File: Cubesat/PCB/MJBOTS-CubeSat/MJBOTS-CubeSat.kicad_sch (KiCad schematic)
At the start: 11 parts, among them J1 Li 24V Battery, J2 MPU 6050, J3 Conn_01x08, J4 Conn_02x20_Odd_Even, U1 LM2596S

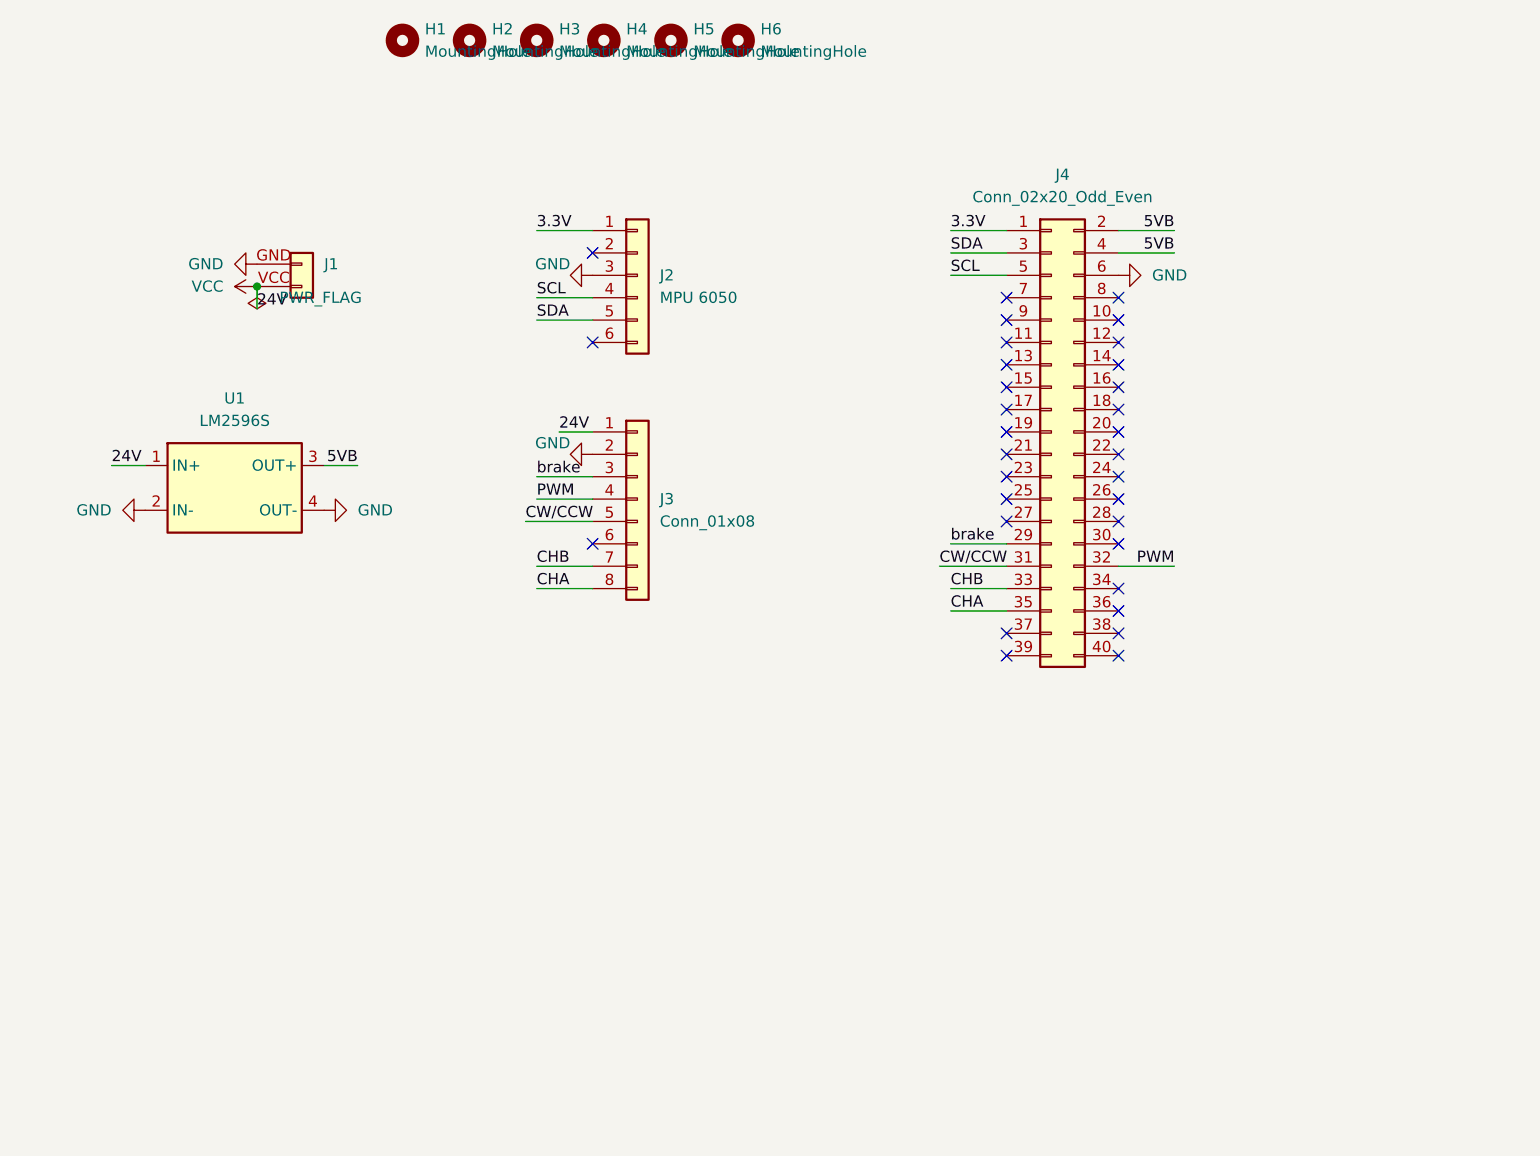
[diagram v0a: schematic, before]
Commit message: Updated Moteus PCB
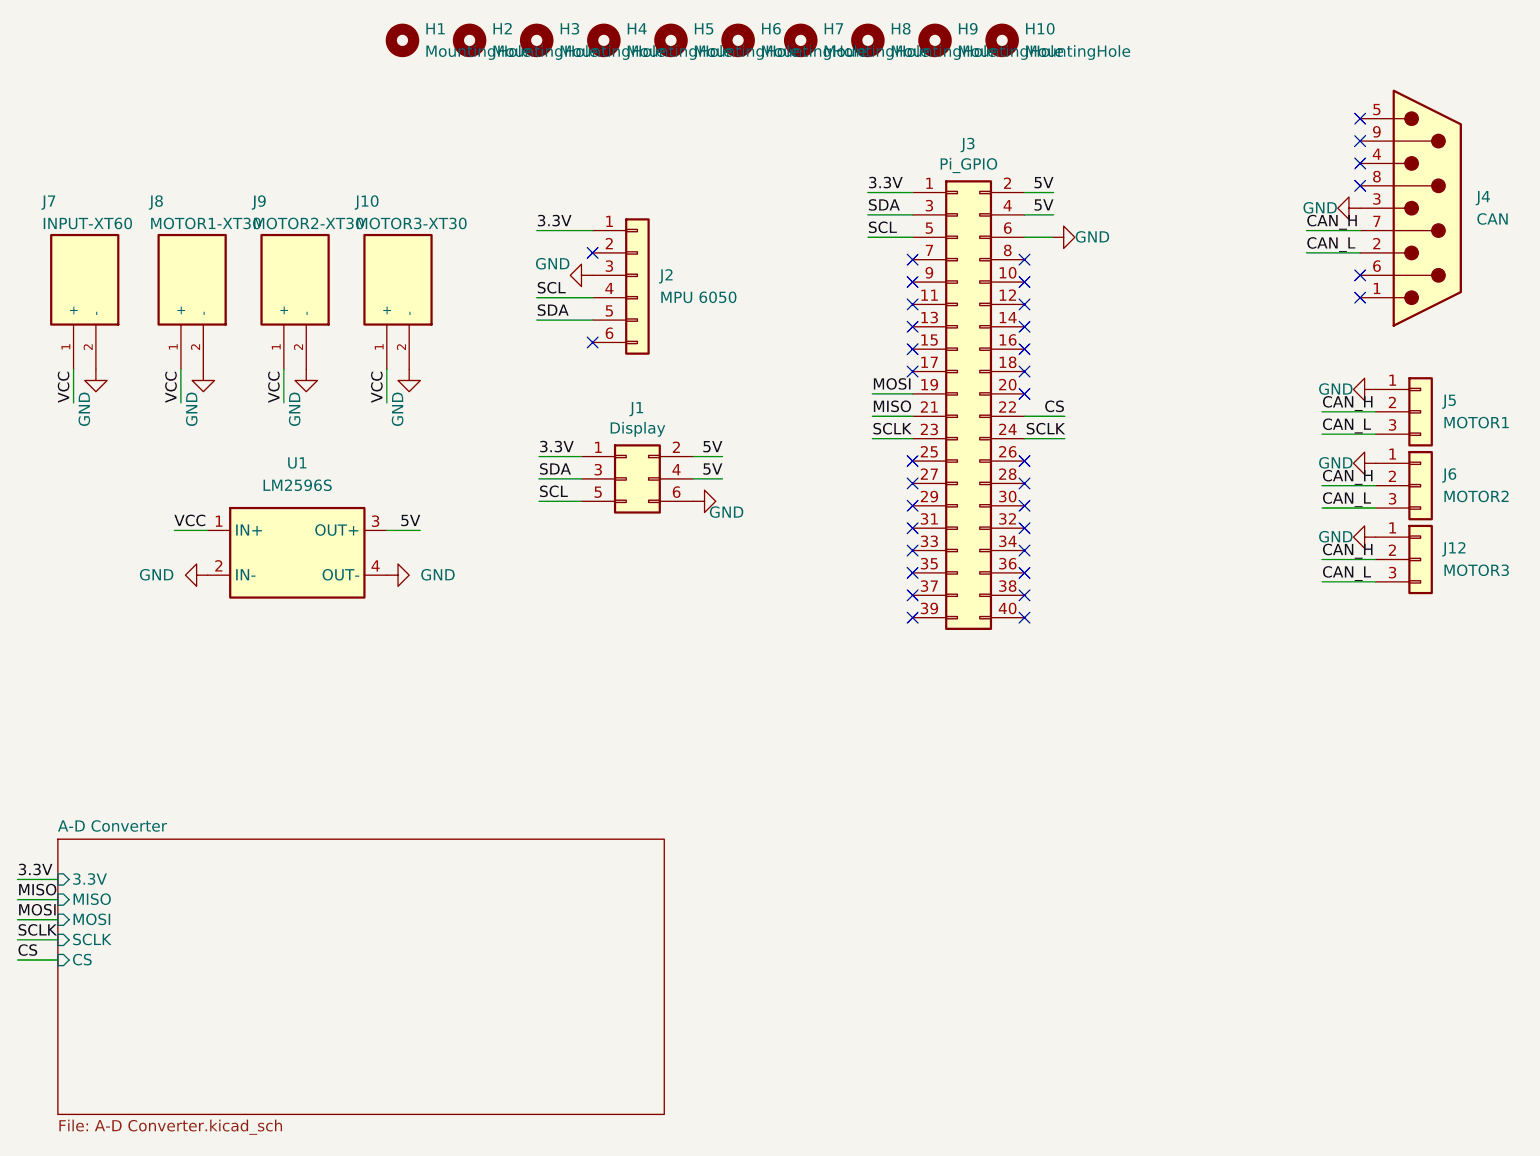
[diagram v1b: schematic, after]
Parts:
- removed J1: Li 24V Battery, cube:24V_Li_batt, symbol 24V_Li_batt:Li 24V Battery
- removed J3: Conn_01x08, Connector_PinHeader_2.54mm:PinHeader_1x08_P2.54mm_Vertical, symbol 24V_Li_batt:Conn_01x08
- removed J4: Conn_02x20_Odd_Even, Connector_PinHeader_2.54mm:PinHeader_2x20_P2.54mm_Vertical, symbol 24V_Li_batt:Conn_02x20_Odd_Even
- added H10, H7, H8, H9: MountingHole, MountingHole:MountingHole_2.5mm, symbol Mechanical:MountingHole
- added J1: Display, Connector_PinHeader_2.54mm:PinHeader_2x03_P2.54mm_Vertical, symbol Connector_Generic:Conn_02x03_Odd_Even
- added J10: MOTOR3-XT30, cube:XT30PWM, symbol XT60PW-M:XT60PW-M
- added J12: MOTOR3, Connector_PinHeader_2.54mm:PinHeader_1x03_P2.54mm_Vertical, symbol 24V_Li_batt:Conn_01x03
- added J3: Pi_GPIO, Connector_PinHeader_2.54mm:PinHeader_2x20_P2.54mm_Vertical, symbol Connector_Generic:Conn_02x20_Odd_Even
- added J4: CAN, Connector_Dsub:DSUB-9_Male_Vertical_P2.77x2.84mm, symbol Connector:DB9_Male
- added J5: MOTOR1, Connector_PinHeader_2.54mm:PinHeader_1x03_P2.54mm_Vertical, symbol 24V_Li_batt:Conn_01x03
- added J6: MOTOR2, Connector_PinHeader_2.54mm:PinHeader_1x03_P2.54mm_Vertical, symbol 24V_Li_batt:Conn_01x03
- added J7: INPUT-XT60, cube:AMASS_XT60PW-M, symbol XT60PW-M:XT60PW-M
- added J8: MOTOR1-XT30, cube:XT30PWM, symbol XT60PW-M:XT60PW-M
- added J9: MOTOR2-XT30, cube:XT30PWM, symbol XT60PW-M:XT60PW-M
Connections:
- net 3.3V: now also J1.1 (Pin_1), J3.1 (Pin_1)
- net GND: now also J1.6 (Pin_6), J10.2 (-), J12.1 (Pin_1), J3.6 (Pin_6), J4.3, J5.1 (Pin_1), J6.1 (Pin_1), J7.2 (-), J8.2 (-), J9.2 (-)
- net SCL: now also J1.5 (Pin_5), J3.5 (Pin_5)
- net SDA: now also J1.3 (Pin_3), J3.3 (Pin_3)
- net VCC: now also J10.1 (+), J7.1 (+), J8.1 (+), J9.1 (+)
- net 5VB renamed 5V
- net 5V: now also J1.2 (Pin_2), J1.4 (Pin_4), J3.2 (Pin_2), J3.4 (Pin_4)
- new net CAN_H: J12.2 (Pin_2), J4.7, J5.2 (Pin_2), J6.2 (Pin_2)
- new net CAN_L: J12.3 (Pin_3), J4.2, J5.3 (Pin_3), J6.3 (Pin_3)
- new net CS: J3.22 (Pin_22)
- new net MISO: J3.21 (Pin_21)
- new net MOSI: J3.19 (Pin_19)
- new net SCLK: J3.23 (Pin_23), J3.24 (Pin_24)
- no-connect marks 32 -> 37
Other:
- added sheet A-D Converter (A-D Converter.kicad_sch)
- moved on the sheet: U1
